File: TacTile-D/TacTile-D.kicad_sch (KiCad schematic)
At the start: 8 parts, among them J18 Conn_01x06, J19 Conn_01x06, J20 Conn_01x06, J21 Conn_01x06, U12 74HC595, U13 74HC590, U18 74LVC2G04, U6 74LVC2G08

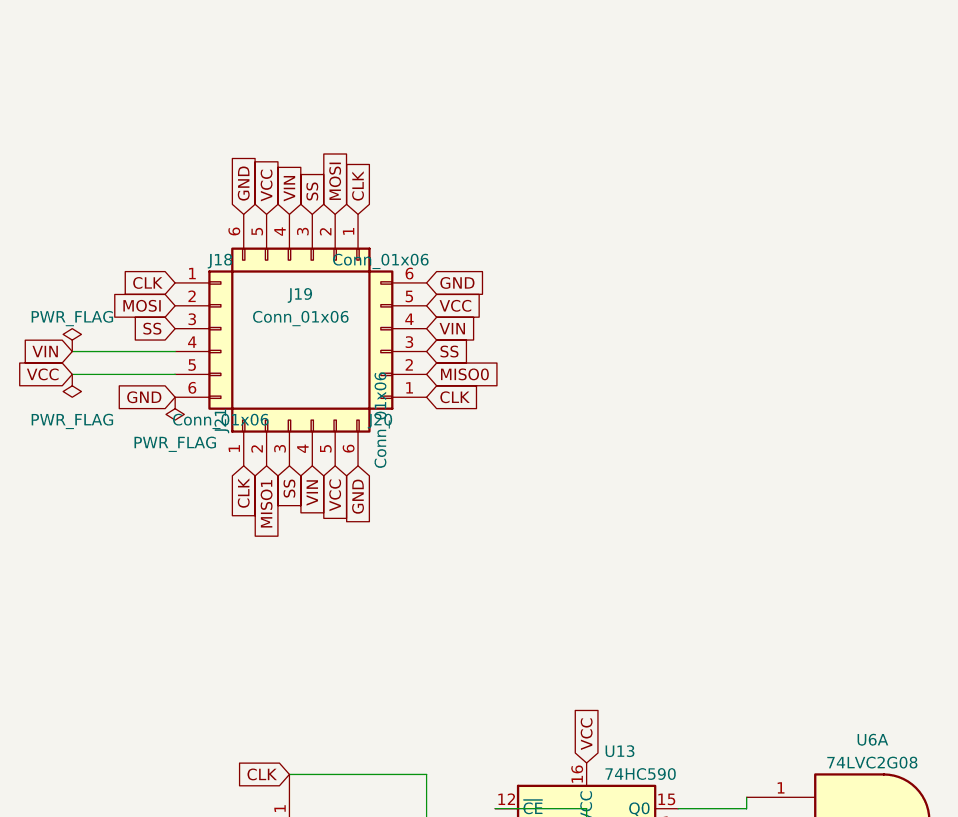
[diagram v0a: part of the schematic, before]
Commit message: Selected and placed footprints for board D
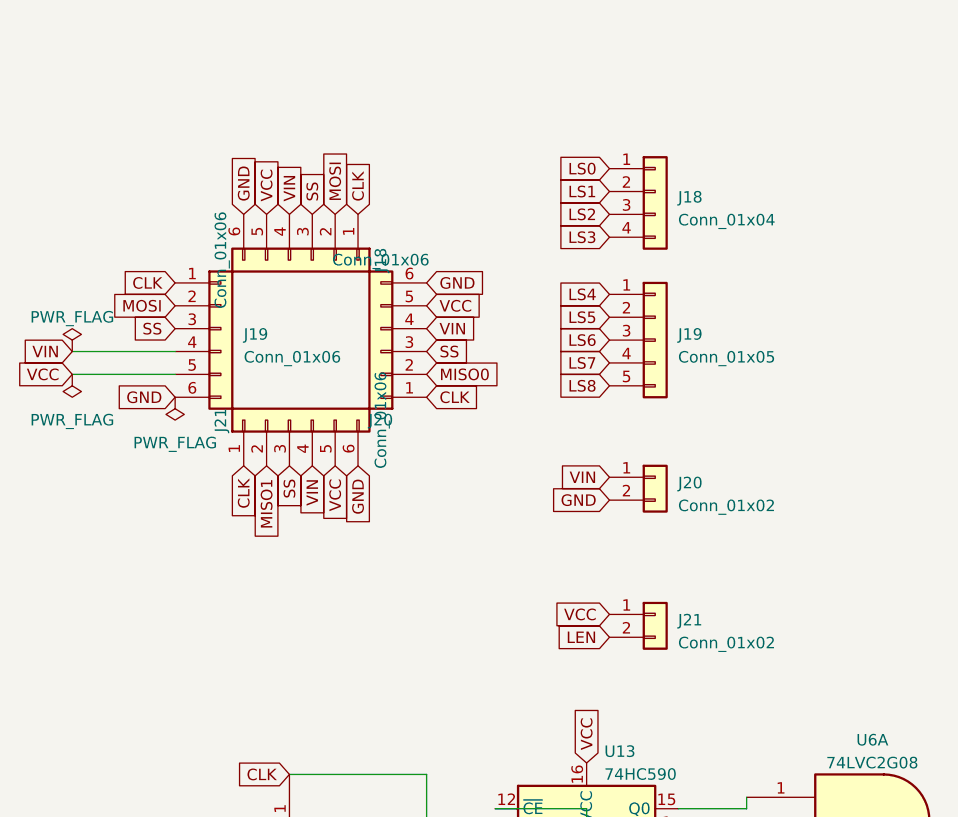
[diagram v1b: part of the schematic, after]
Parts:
- added J18: Conn_01x04, Connector_PinSocket_1.27mm:PinSocket_1x04_P1.27mm_Vertical, symbol Connector_Generic:Conn_01x04
- added J19: Conn_01x05, Connector_PinSocket_1.27mm:PinSocket_1x05_P1.27mm_Vertical, symbol Connector_Generic:Conn_01x05
- added J20, J21: Conn_01x02, Connector_PinSocket_1.27mm:PinSocket_1x02_P1.27mm_Vertical, symbol Connector_Generic:Conn_01x02
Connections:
- net GND: now also J20.2 (Pin_2)
- net LEN: now also J21.2 (Pin_2)
- net LS0: now also J18.1 (Pin_1)
- net LS1: now also J18.2 (Pin_2)
- net LS2: now also J18.3 (Pin_3)
- net LS3: now also J18.4 (Pin_4)
- net LS4: now also J19.1 (Pin_1)
- net LS5: now also J19.2 (Pin_2)
- net LS6: now also J19.3 (Pin_3)
- net LS7: now also J19.4 (Pin_4)
- net LS8: now also J19.5 (Pin_5)
- net VCC: now also J21.1 (Pin_1)
- net VIN: now also J20.1 (Pin_1)
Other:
- moved on the sheet: J18, J19

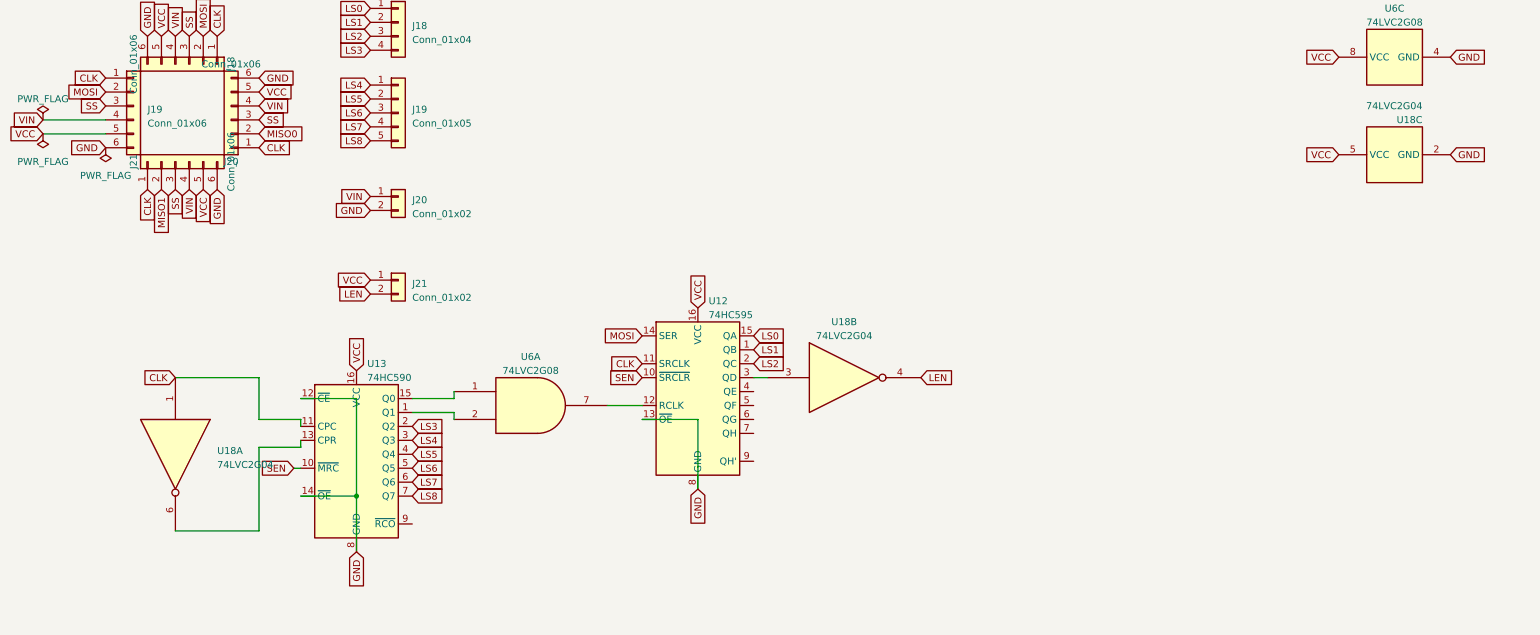
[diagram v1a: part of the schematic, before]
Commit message: Ensured outputs were disabled on reset - added not gate
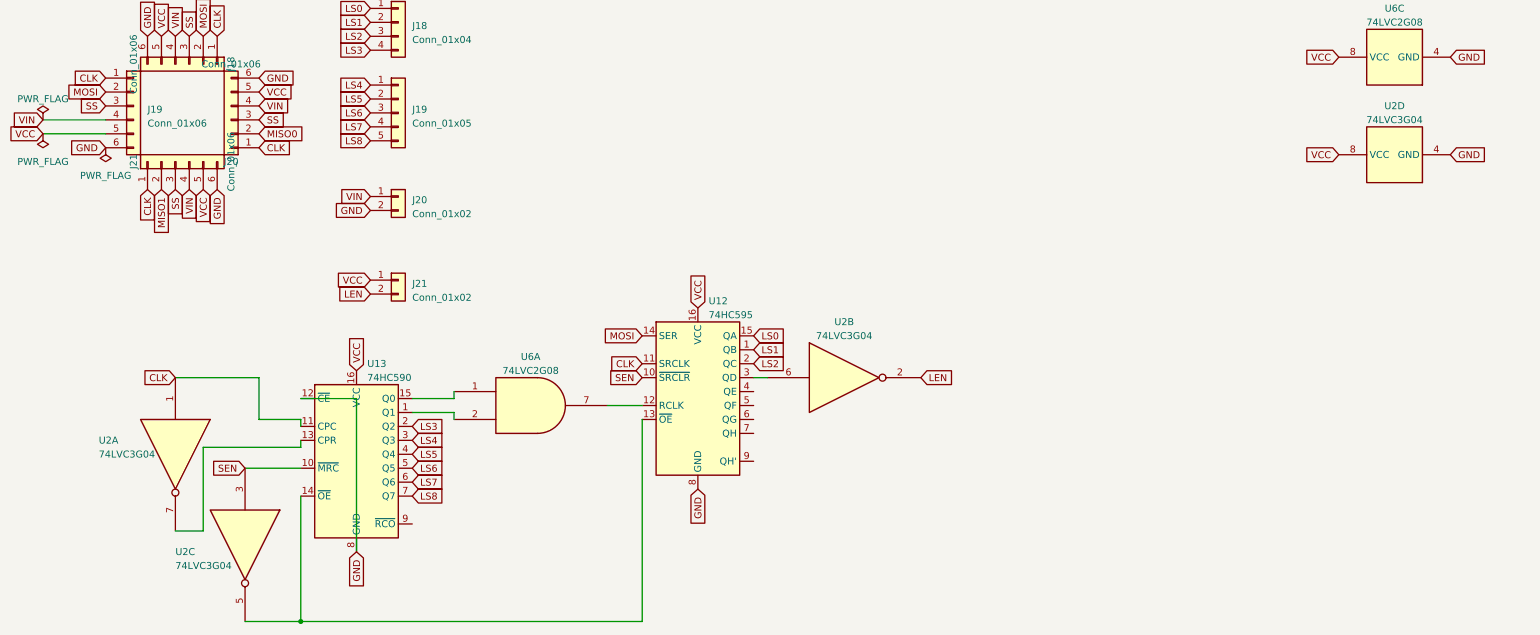
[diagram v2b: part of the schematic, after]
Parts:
- removed U18: 74LVC2G04, Package_DIP:DIP-6_W7.62mm_Socket, symbol 74xGxx:74LVC2G04
- added U2: 74LVC3G04, Package_DIP:DIP-8_W7.62mm_Socket, symbol 74xGxx:74LVC3G04
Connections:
- net CLK: now also U2.1
- net GND: now also U2.4 (GND); no longer U12.13 (~{OE}), U13.14 (~{OE})
- net LEN: now also U2.2
- net SEN: now also U2.3
- net VCC: now also U2.8 (VCC)
- net at U12.3 (QD): now also U2.6
- net at U13.13 (CPR): now also U2.7
- new net: U12.13 (~{OE}), U13.14 (~{OE}), U2.5
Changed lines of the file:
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@@
 (kicad_sch (version 20230121) (generator eeschema)
   (paper "A4")
-  (junction (at 77.47 105.41) (diameter 0) (color 0 0 0 0)
+  (junction (at 67.31 128.27) (diameter 0) (color 0 0 0 0)
+  )
+  (wire (pts (xy 67.31 128.27) (xy 129.54 128.27))
+    (stroke (width 0) (type default))
   )
   (wire (pts (xy 67.31 91.44) (xy 67.31 92.71))
@@
     (stroke (width 0) (type default))
   )
-  (wire (pts (xy 59.69 96.52) (xy 67.31 96.52))
-    (stroke (width 0) (type default))
-  )
-  (wire (pts (xy 129.54 91.44) (xy 139.7 91.44))
+  (wire (pts (xy 49.53 96.52) (xy 67.31 96.52))
+    (stroke (width 0) (type default))
+  )
+  (wire (pts (xy 129.54 128.27) (xy 129.54 91.44))
     (stroke (width 0) (type default))
   )
@@
     (stroke (width 0) (type default))
   )
-  (wire (pts (xy 66.04 100.33) (xy 67.31 100.33))
-    (stroke (width 0) (type default))
-  )
-  (wire (pts (xy 77.47 87.63) (xy 77.47 105.41))
+  (wire (pts (xy 57.15 100.33) (xy 67.31 100.33))
+    (stroke (width 0) (type default))
+  )
+  (wire (pts (xy 77.47 87.63) (xy 77.47 115.57))
     (stroke (width 0) (type default))
   )
@@
     (stroke (width 0) (type default))
   )
+  (wire (pts (xy 67.31 128.27) (xy 67.31 105.41))
+    (stroke (width 0) (type default))
+  )
   (wire (pts (xy 20.32 39.37) (xy 31.75 39.37))
     (stroke (width 0) (type default))
   )
-  (wire (pts (xy 67.31 105.41) (xy 77.47 105.41))
-    (stroke (width 0) (type default))
-  )
-  (wire (pts (xy 59.69 111.76) (xy 59.69 96.52))
+  (wire (pts (xy 49.53 111.76) (xy 49.53 96.52))
     (stroke (width 0) (type default))
   )
@@
     (stroke (width 0) (type default))
   )
+  (wire (pts (xy 57.15 128.27) (xy 67.31 128.27))
+    (stroke (width 0) (type default))
+  )
   (wire (pts (xy 67.31 87.63) (xy 77.47 87.63))
     (stroke (width 0) (type default))
   )
-  (wire (pts (xy 139.7 91.44) (xy 139.7 104.14))
-    (stroke (width 0) (type default))
-  )
-  (wire (pts (xy 77.47 105.41) (xy 77.47 115.57))
-    (stroke (width 0) (type default))
-  )
   (wire (pts (xy 87.63 90.17) (xy 95.25 90.17))
     (stroke (width 0) (type default))
   )
-  (wire (pts (xy 44.45 111.76) (xy 59.69 111.76))
+  (wire (pts (xy 44.45 111.76) (xy 49.53 111.76))
     (stroke (width 0) (type default))
   )
@@
     )
   )
-  (global_label "SEN" (shape input) (at 66.04 100.33 180) (fields_autoplaced)
-    (effects (font (size 1.27 1.27)) (justify right))
-    (property "Intersheetrefs" "${INTERSHEET_REFS}" (at 59.4452 100.33 0)
+  (global_label "SEN" (shape input) (at 57.15 100.33 180) (fields_autoplaced)
+    (effects (font (size 1.27 1.27)) (justify right))
+    (property "Intersheetrefs" "${INTERSHEET_REFS}" (at 50.5552 100.33 0)
       (effects (font (size 1.27 1.27)) (justify right) hide)
     )
@@
     )
   )
-  (symbol (lib_id "74xGxx:74LVC2G04") (at 266.7 43.18 90) (unit 3)
-    (in_bom yes) (on_board yes) (dnp no)
-    (property "Reference" "U18" (at 271.78 36.83 90)
-      (effects (font (size 1.27 1.27)) (justify left))
-    )
-    (property "Value" "74LVC2G04" (at 271.78 34.29 90)
-      (effects (font (size 1.27 1.27)) (justify left))
-    )
-    (property "Footprint" "Package_DIP:DIP-6_W7.62mm_Socket" (at 266.7 43.18 0)
-      (effects (font (size 1.27 1.27)) hide)
-    )
-    (property "Datasheet" "http://www.ti.com/lit/sg/scyt129e/scyt129e.pdf" (at 266.7 43.18 0)
-      (effects (font (size 1.27 1.27)) hide)
-    )
-    (pin "1")
-    (pin "6")
-    (pin "3")
-    (pin "4")
-    (pin "2")
-    (pin "5")
-    (instances
-      (project "TacTile-C"
-        (path "/36638316-989c-497b-a9a8-6f6d869c219d/11cf69d3-b8f7-4559-98b1-f219145c2513"
-          (reference "U18") (unit 3)
-        )
-        (path "/36638316-989c-497b-a9a8-6f6d869c219d"
-          (reference "U11") (unit 3)
-        )
-      )
-      (project "TacTile-D"
-        (path "/99b9cae1-6ece-4124-abcb-60ec0df49dce"
-          (reference "U2") (unit 3)
-        )
-      )
-    )
-  )
   (symbol (lib_id "power:PWR_FLAG") (at 31.75 41.91 180) (unit 1)
     (in_bom yes) (on_board yes) (dnp no) (fields_autoplaced)
@@
     )
   )
+  (symbol (lib_id "74xGxx:74LVC3G04") (at 266.7 43.18 90) (unit 4)
+    (in_bom yes) (on_board yes) (dnp no) (fields_autoplaced)
+    (property "Reference" "U2" (at 266.7 34.29 90)
+      (effects (font (size 1.27 1.27)))
+    )
+    (property "Value" "74LVC3G04" (at 266.7 36.83 90)
+      (effects (font (size 1.27 1.27)))
+    )
+    (property "Footprint" "Package_DIP:DIP-8_W7.62mm_Socket" (at 266.7 43.18 0)
+      (effects (font (size 1.27 1.27)) hide)
+    )
+    (property "Datasheet" "http://www.ti.com/lit/sg/scyt129e/scyt129e.pdf" (at 266.7 43.18 0)
+      (effects (font (size 1.27 1.27)) hide)
+    )
+    (pin "1")
+    (pin "7")
+    (pin "2")
+    (pin "6")
+    (pin "3")
+    (pin "5")
+    (pin "4")
+    (pin "8")
+    (instances
+      (project "TacTile-D"
+        (path "/99b9cae1-6ece-4124-abcb-60ec0df49dce"
+          (reference "U2") (unit 4)
+        )
+      )
+    )
+  )
   (symbol (lib_id "Connector_Generic:Conn_01x02") (at 85.09 66.04 0) (unit 1)
     (in_bom yes) (on_board yes) (dnp no) (fields_autoplaced)
@@
     )
   )
-  (symbol (lib_id "74xGxx:74LVC2G04") (at 167.64 83.82 0) (unit 2)
-    (in_bom yes) (on_board yes) (dnp no) (fields_autoplaced)
-    (property "Reference" "U18" (at 166.37 73.66 0)
-      (effects (font (size 1.27 1.27)))
-    )
-    (property "Value" "74LVC2G04" (at 166.37 76.2 0)
-      (effects (font (size 1.27 1.27)))
-    )
-    (property "Footprint" "Package_DIP:DIP-6_W7.62mm_Socket" (at 167.64 83.82 0)
+  (symbol (lib_id "74xGxx:74LVC3G04") (at 167.64 83.82 0) (unit 2)
+    (in_bom yes) (on_board yes) (dnp no) (fields_autoplaced)
+    (property "Reference" "U2" (at 166.37 73.66 0)
+      (effects (font (size 1.27 1.27)))
+    )
+    (property "Value" "74LVC3G04" (at 166.37 76.2 0)
+      (effects (font (size 1.27 1.27)))
+    )
+    (property "Footprint" "Package_DIP:DIP-8_W7.62mm_Socket" (at 167.64 83.82 0)
       (effects (font (size 1.27 1.27)) hide)
     )
@@
     )
     (pin "1")
+    (pin "7")
+    (pin "2")
     (pin "6")
     (pin "3")
-    (pin "4")
-    (pin "2")
-    (pin "5")
-    (instances
-      (project "TacTile-C"
-        (path "/36638316-989c-497b-a9a8-6f6d869c219d/11cf69d3-b8f7-4559-98b1-f219145c2513"
-          (reference "U18") (unit 2)
-        )
-        (path "/36638316-989c-497b-a9a8-6f6d869c219d"
-          (reference "U11") (unit 2)
-        )
-      )
+    (pin "5")
+    (pin "4")
+    (pin "8")
+    (instances
       (project "TacTile-D"
         (path "/99b9cae1-6ece-4124-abcb-60ec0df49dce"
           (reference "U2") (unit 2)
+        )
+      )
+    )
+  )
+  (symbol (lib_id "74xGxx:74LVC3G04") (at 57.15 115.57 270) (unit 3)
+    (in_bom yes) (on_board yes) (dnp no)
+    (property "Reference" "U2" (at 44.45 115.57 90)
+      (effects (font (size 1.27 1.27)) (justify left))
+    )
+    (property "Value" "74LVC3G04" (at 44.45 118.11 90)
+      (effects (font (size 1.27 1.27)) (justify left))
+    )
+    (property "Footprint" "Package_DIP:DIP-8_W7.62mm_Socket" (at 57.15 115.57 0)
+      (effects (font (size 1.27 1.27)) hide)
+    )
+    (property "Datasheet" "http://www.ti.com/lit/sg/scyt129e/scyt129e.pdf" (at 57.15 115.57 0)
+      (effects (font (size 1.27 1.27)) hide)
+    )
+    (pin "1")
+    (pin "7")
+    (pin "2")
+    (pin "6")
+    (pin "3")
+    (pin "5")
+    (pin "4")
+    (pin "8")
+    (instances
+      (project "TacTile-D"
+        (path "/99b9cae1-6ece-4124-abcb-60ec0df49dce"
+          (reference "U2") (unit 3)
         )
       )
@@
     )
   )
-  (symbol (lib_id "74xGxx:74LVC2G04") (at 44.45 99.06 270) (unit 1)
-    (in_bom yes) (on_board yes) (dnp no) (fields_autoplaced)
-    (property "Reference" "U18" (at 52.07 97.155 90)
-      (effects (font (size 1.27 1.27)) (justify left))
-    )
-    (property "Value" "74LVC2G04" (at 52.07 99.695 90)
-      (effects (font (size 1.27 1.27)) (justify left))
-    )
-    (property "Footprint" "Package_DIP:DIP-6_W7.62mm_Socket" (at 44.45 99.06 0)
+  (symbol (lib_id "74xGxx:74LVC3G04") (at 44.45 99.06 270) (unit 1)
+    (in_bom yes) (on_board yes) (dnp no)
+    (property "Reference" "U2" (at 30.48 95.25 90)
+      (effects (font (size 1.27 1.27)) (justify left))
+    )
+    (property "Value" "74LVC3G04" (at 30.48 97.79 90)
+      (effects (font (size 1.27 1.27)) (justify left))
+    )
+    (property "Footprint" "Package_DIP:DIP-8_W7.62mm_Socket" (at 44.45 99.06 0)
       (effects (font (size 1.27 1.27)) hide)
     )
@@
     )
     (pin "1")
+    (pin "7")
+    (pin "2")
     (pin "6")
     (pin "3")
-    (pin "4")
-    (pin "2")
-    (pin "5")
-    (instances
-      (project "TacTile-C"
-        (path "/36638316-989c-497b-a9a8-6f6d869c219d/11cf69d3-b8f7-4559-98b1-f219145c2513"
-          (reference "U18") (unit 1)
-        )
-        (path "/36638316-989c-497b-a9a8-6f6d869c219d"
-          (reference "U11") (unit 1)
-        )
-      )
-      (project "TacTile-D"
-        (path "/99b9cae1-6ece-4124-abcb-60ec0df49dce"
+    (pin "5")
+    (pin "4")
+    (pin "8")
+    (instances
+      (project "TacTile-D"
+        (path "/99b9cae1-6ece-4124-abcb-60ec0df49dce"

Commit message: Mounted ICs without sockets to save space
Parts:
- U12, U13: footprint Package_DIP:DIP-16_W7.62mm_Socket -> Package_DIP:DIP-16_W7.62mm
- U2, U6: footprint Package_DIP:DIP-8_W7.62mm_Socket -> Package_DIP:DIP-8_W7.62mm
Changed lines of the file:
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@@
       (effects (font (size 1.27 1.27)) (justify left))
     )
-    (property "Footprint" "Package_DIP:DIP-16_W7.62mm_Socket" (at 139.7 86.36 0)
+    (property "Footprint" "Package_DIP:DIP-16_W7.62mm" (at 139.7 86.36 0)
       (effects (font (size 1.27 1.27)) hide)
     )
@@
       (effects (font (size 1.27 1.27)))
     )
-    (property "Footprint" "Package_DIP:DIP-8_W7.62mm_Socket" (at 266.7 25.4 0)
+    (property "Footprint" "Package_DIP:DIP-8_W7.62mm" (at 266.7 25.4 0)
       (effects (font (size 1.27 1.27)) hide)
     )
@@
       (effects (font (size 1.27 1.27)))
     )
-    (property "Footprint" "Package_DIP:DIP-8_W7.62mm_Socket" (at 266.7 43.18 0)
+    (property "Footprint" "Package_DIP:DIP-8_W7.62mm" (at 266.7 43.18 0)
       (effects (font (size 1.27 1.27)) hide)
     )
@@
       (effects (font (size 1.27 1.27)))
     )
-    (property "Footprint" "Package_DIP:DIP-8_W7.62mm_Socket" (at 167.64 83.82 0)
+    (property "Footprint" "Package_DIP:DIP-8_W7.62mm" (at 167.64 83.82 0)
       (effects (font (size 1.27 1.27)) hide)
     )
@@
       (effects (font (size 1.27 1.27)) (justify left))
     )
-    (property "Footprint" "Package_DIP:DIP-8_W7.62mm_Socket" (at 57.15 115.57 0)
+    (property "Footprint" "Package_DIP:DIP-8_W7.62mm" (at 57.15 115.57 0)
       (effects (font (size 1.27 1.27)) hide)
     )
@@
       (effects (font (size 1.27 1.27)))
     )
-    (property "Footprint" "Package_DIP:DIP-8_W7.62mm_Socket" (at 110.49 88.9 0)
+    (property "Footprint" "Package_DIP:DIP-8_W7.62mm" (at 110.49 88.9 0)
       (effects (font (size 1.27 1.27)) hide)
     )
@@
       (effects (font (size 1.27 1.27)) (justify left))
     )
-    (property "Footprint" "Package_DIP:DIP-8_W7.62mm_Socket" (at 44.45 99.06 0)
+    (property "Footprint" "Package_DIP:DIP-8_W7.62mm" (at 44.45 99.06 0)
       (effects (font (size 1.27 1.27)) hide)
     )
@@
       (effects (font (size 1.27 1.27)) (justify left))
     )
-    (property "Footprint" "Package_DIP:DIP-16_W7.62mm_Socket" (at 77.47 99.06 0)
-      (effects (font (size 1.27 1.27)) hide)
-    )
+    (property "Footprint" "Package_DIP:DIP-16_W7.62mm" (at 77.47 99.06 0)
+      (effects (font (size 1.27 1.27)) hide)
+    )
